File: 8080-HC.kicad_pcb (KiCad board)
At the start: 4 copper layers, 349 parts, among them U1 74HCU04, U10 74HC00, U11 74HC126, U12 74HC161, U13 74HC238, U14 74HC238, U15 74HC238, U16 74HC238, U17 74HC04, U178 74LS03, U18 74HC05, U181 74HC244, U182 74HC244, U19 74HC74, U194 74HC244, U195 74HC244, U2 74HC74, U20 74HC373, U21 74HC373, U215 74HC193, U216 74HC193, U217 74HC193, U218 74HC193, U22 74HC373, U23 74HC373, U239 74HC74, U24 74HC373, U242 74HC00, U243 74HCU04, U244 74HC00, U25 74HC244, U26 74HC244, U27 74HC244, U28 74HC244, U29 74HC244, U3 74HC00, U30 74HC373, U31 74HC373, U32 74HC244, U33 74HC244, U34 74HC244, U35 74HC244, U36 74HC373, U37 74HC373, U38 74HC244, U39 74HC244, U4 74HC04, U40 74HC244, U41 74HC244, U42 74HC245, U43 74HC04, U44 74HC04, U45 74LS373, U46 74HC04, U47 74HC04, U48 74HC04, U49 74HC04, U5 74HC00, U50 74HC04, U51 74HC04, U52 74HC04, U53 74HC238, U54 74HC238, U55 74HC238, U56 74HC238, U57 74HC04, U58 74HC04, U6 74HC04, U69 74HC05, U7 74HC05, U70 74LS05, U71 74HC04, U72 74LS126, U73 74LS126, U74 74LS126, U75 74LS126, U76 74LS126, U77 74HC00, U78 74HC00, U79 74HC04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

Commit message: finish routing the PC module
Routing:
- net iB6: track 52.8 -> 157.9 mm, vias 3 -> 8
- net iB5: track 86.3 -> 136.1 mm, vias 3 -> 5
- net Net-(L221-Pad2): track 12.5 -> 59.6 mm, vias 0 -> 5
- net Net-(L214-Pad2): track 12.5 -> 54.2 mm, vias 0 -> 2
- net Net-(L215-Pad2): track 12.9 -> 53.8 mm, vias 0 -> 3
- net Net-(L224-Pad2): track 21.7 -> 59.3 mm, vias 1 -> 2
- net iB1: track 97.0 -> 134.0 mm, vias 2 -> 3
- net Net-(L225-Pad2): track 28.5 -> 64.4 mm, vias 2 -> 5
- net Net-(L220-Pad2): track 51.0 -> 85.5 mm, vias 2 -> 4
- net Net-(L213-Pad2): track 29.0 -> 60.0 mm, vias 0 -> 2
- net Net-(L212-Pad2): track 42.0 -> 71.8 mm, vias 2 -> 4
- net Net-(L210-Pad2): track 56.4 -> 85.1 mm, vias 2 -> 3
- net Net-(L223-Pad2): track 31.9 -> 56.9 mm, vias 2 -> 4
- net Net-(L211-Pad2): track 47.7 -> 72.0 mm, vias 1 -> 2
- net Net-(L216-Pad2): track 33.8 -> 55.4 mm, vias 2 -> 3
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
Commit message: start routing the OPcode register, we have a piece of the iBn bus
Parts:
- removed D107, D109, D111, D114, D117, D120, D123, D125: LED_Small_ALT, LED_THT:LED_D3.0mm
- added L264: LED_Small_ALT, LED_THT:LED_D3.0mm, F.Cu at (-174.6, -19.1)
- added L265: LED_Small_ALT, LED_THT:LED_D3.0mm, F.Cu at (-170.1, -19.1)
- added L266: LED_Small_ALT, LED_THT:LED_D3.0mm, F.Cu at (-165.5, -19.1)
- added L267: LED_Small_ALT, LED_THT:LED_D3.0mm, F.Cu at (-160.9, -19.1)
- added L268: LED_Small_ALT, LED_THT:LED_D3.0mm, F.Cu at (-156.3, -19.1)
- added L269: LED_Small_ALT, LED_THT:LED_D3.0mm, F.Cu at (-151.8, -19.1)
- added L270: LED_Small_ALT, LED_THT:LED_D3.0mm, F.Cu at (-147.2, -19.1)
- added L271: LED_Small_ALT, LED_THT:LED_D3.0mm, F.Cu at (-142.6, -19.1)
- B37: renamed from RN17; value R_Network08 -> 22K
- moved B37 504.1 mm to (-148.6, -26.7), turned to 180 degrees
- moved U234 481.8 mm to (-170.2, -30.5), turned to 90 degrees
- moved D7 270.2 mm to (-130.0, -214.0)
- moved D79 270.2 mm to (66.2, -291.1)
- moved D85 270.2 mm to (65.9, -296.6)
- moved R19 270.2 mm to (46.6, -297.4)
- moved U36 270.2 mm to (76.1, -324.3)
- moved U58 270.2 mm to (146.5, -324.3)
- moved U90 270.2 mm to (70.9, -257.1)
- moved C1 270.2 mm to (-126.8, -281.7)
- moved C4 270.2 mm to (-10.9, -155.6)
- moved D1 270.2 mm to (-108.3, -237.8)
- moved D10 270.2 mm to (-83.5, -259.0)
- moved D100 270.2 mm to (-92.4, -298.7)
- moved D101 270.2 mm to (-98.3, -293.1)
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- renumbered U45 to U234
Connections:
- B38 pad 2: (no net) -> Net-(B38-Pad2)
- B38 pad 3: (no net) -> Net-(B38-Pad3)
- B38 pad 4: (no net) -> Net-(B38-Pad4)
- B38 pad 5: (no net) -> Net-(B38-Pad5)
- B38 pad 8: (no net) -> Net-(B38-Pad8)
- B38 pad 9: (no net) -> Net-(B38-Pad9)
- L218 pad 1: (no net) -> Net-(L218-Pad1)
- L277 pad 1: (no net) -> BUSAK
- RN15 pad 2: /I/O regs/iB0 -> iB0
- RN15 pad 3: /I/O regs/iB1 -> iB1
- RN15 pad 4: /I/O regs/iB2 -> iB2
- RN15 pad 5: /I/O regs/iB3 -> iB3
- RN15 pad 6: /I/O regs/iB4 -> iB4
- RN15 pad 7: /I/O regs/iB5 -> iB5
- RN15 pad 8: /I/O regs/iB6 -> iB6
- RN15 pad 9: /I/O regs/iB7 -> iB7
- U10 pad 10: (no net) -> Net-(U10-Pad10)
- U10 pad 11: (no net) -> Net-(U10-Pad11)
- U10 pad 12: (no net) -> Net-(U10-Pad12)
- U10 pad 13: (no net) -> Net-(U10-Pad13)
- U10 pad 8: (no net) -> Net-(U10-Pad8)
- U10 pad 9: (no net) -> Net-(U10-Pad9)
- U11 pad 1: (no net) -> Net-(U11-Pad1)
- U11 pad 11: (no net) -> /Timings Generator/QC
- U11 pad 3: (no net) -> /Timings Generator/QA
- U11 pad 6: (no net) -> /Timings Generator/QB
- U11 pad 8: (no net) -> /Timings Generator/QD
- U12 pad 2: (no net) -> /Timings Generator/CLK
- U13 pad 10: (no net) -> Net-(U13-Pad10)
- U13 pad 11: (no net) -> Net-(U13-Pad11)
- U13 pad 12: (no net) -> Net-(U13-Pad12)
- U13 pad 13: (no net) -> /Timings Generator/W2
- U13 pad 14: (no net) -> /Timings Generator/W1
- U13 pad 15: (no net) -> /Timings Generator/W0
- U13 pad 7: (no net) -> Net-(U13-Pad7)
- U13 pad 9: (no net) -> Net-(U13-Pad9)
- U14 pad 10: (no net) -> Net-(U14-Pad10)
- U14 pad 11: (no net) -> Net-(U14-Pad11)
- U14 pad 12: (no net) -> Net-(U14-Pad12)
- U14 pad 13: (no net) -> /Timings Generator/M2
- U14 pad 14: (no net) -> Net-(U14-Pad14)
- U14 pad 15: (no net) -> Net-(U14-Pad15)
- U14 pad 7: (no net) -> Net-(U14-Pad7)
- U14 pad 9: (no net) -> Net-(U14-Pad9)
- U15 pad 10: (no net) -> Net-(U15-Pad10)
- U15 pad 11: (no net) -> /Timings Generator/T12
- U15 pad 12: (no net) -> Net-(U15-Pad12)
- U15 pad 13: (no net) -> /Timings Generator/T10
- U15 pad 14: (no net) -> /Timings Generator/T9
- U15 pad 15: (no net) -> /Timings Generator/T8
- U15 pad 7: (no net) -> Net-(U15-Pad7)
- U15 pad 9: (no net) -> Net-(U15-Pad9)
- U16 pad 10: (no net) -> /Timings Generator/T5
- U16 pad 11: (no net) -> /Timings Generator/T4
- U16 pad 12: (no net) -> /Timings Generator/T3
- U16 pad 13: (no net) -> /Timings Generator/T2
- U16 pad 14: (no net) -> /Timings Generator/T1
- U16 pad 15: (no net) -> /Timings Generator/T0
- U16 pad 7: (no net) -> /Timings Generator/T7
- U16 pad 9: (no net) -> /Timings Generator/T6
- U17 pad 12: (no net) -> Net-(U17-Pad12)
- U17 pad 13: (no net) -> Net-(U17-Pad13)
- U178 pad 4: (no net) -> PCCKdE
- U178 pad 5: (no net) -> T3
- U18 pad 10: (no net) -> Net-(U18-Pad10)
- U18 pad 11: (no net) -> Net-(U18-Pad11)
- U18 pad 12: (no net) -> Net-(U18-Pad12)
- U18 pad 13: (no net) -> Net-(U18-Pad13)
- U18 pad 4: (no net) -> /regs_decode/dataOUT
- U18 pad 8: (no net) -> /regs_decode/memRD
- U181 pad 12: (no net) -> /Program Counter/A11
- U181 pad 14: (no net) -> /Program Counter/A10
- U181 pad 16: (no net) -> /Program Counter/A9
- U181 pad 18: (no net) -> /Program Counter/A8
- U181 pad 3: (no net) -> /Program Counter/A12
- U181 pad 5: (no net) -> /Program Counter/A13
- U181 pad 7: (no net) -> /Program Counter/A14
- U181 pad 9: (no net) -> Net-(U181-Pad9)
- U182 pad 12: (no net) -> /Program Counter/A3
- U182 pad 14: (no net) -> /Program Counter/A2
- U182 pad 16: (no net) -> /Program Counter/A1
- U182 pad 18: (no net) -> /Program Counter/A0
- U182 pad 3: (no net) -> /Program Counter/A4
- U182 pad 5: (no net) -> /Program Counter/A5
- U182 pad 7: (no net) -> /Program Counter/A6
- U182 pad 9: (no net) -> /Program Counter/A7
- U19 pad 10: (no net) -> Net-(U19-Pad10)
- U19 pad 11: (no net) -> Net-(U19-Pad11)
- U19 pad 12: (no net) -> Net-(U19-Pad12)
- U19 pad 13: (no net) -> Net-(U19-Pad13)
- U19 pad 5: (no net) -> Net-(U19-Pad5)
- U19 pad 8: (no net) -> Net-(U19-Pad8)
- U19 pad 9: (no net) -> Net-(U19-Pad9)
- U2 pad 9: (no net) -> Net-(U2-Pad9)
- U20 pad 11: (no net) -> /regs_A_B_C_D_E/AregWR
- U21 pad 11: (no net) -> /regs_A_B_C_D_E/BregWR
- U215 pad 12: (no net) -> Net-(U215-Pad12)
- U215 pad 13: (no net) -> Net-(U215-Pad13)
- U216 pad 12: (no net) -> Net-(U216-Pad12)
- U217 pad 12: (no net) -> Net-(U217-Pad12)
- U218 pad 12: (no net) -> Net-(U218-Pad12)
- U22 pad 11: (no net) -> /regs_A_B_C_D_E/CregWR
- U23 pad 11: (no net) -> /regs_A_B_C_D_E/DregWR
- U234 pad 11: (no net) -> /I/O regs/T1
- U234 pad 12: /I/O regs/OP4 -> OP4
- U234 pad 13: /I/O regs/iB4 -> iB4
- U234 pad 14: /I/O regs/iB5 -> iB5
- U234 pad 15: /I/O regs/OP5 -> OP5
- U234 pad 16: /I/O regs/OP6 -> OP6
- U234 pad 17: /I/O regs/iB6 -> iB6
- U234 pad 18: /I/O regs/iB7 -> iB7
- U234 pad 19: /I/O regs/OP7 -> OP7
- U234 pad 2: /I/O regs/OP0 -> OP0
- U234 pad 3: /I/O regs/iB0 -> iB0
- U234 pad 4: /I/O regs/iB1 -> iB1
- U234 pad 5: /I/O regs/OP1 -> OP1
- U234 pad 6: /I/O regs/OP2 -> OP2
- U234 pad 7: /I/O regs/iB2 -> iB2
- U234 pad 8: /I/O regs/iB3 -> iB3
- U234 pad 9: /I/O regs/OP3 -> OP3
- U24 pad 11: (no net) -> /regs_A_B_C_D_E/EregWR
- U242 pad 8: (no net) -> CLK
- U244 pad 11: (no net) -> CLK2
- U244 pad 3: (no net) -> /I/O control/DataDIR
- U3 pad 10: (no net) -> /HALT/T2
- U3 pad 9: (no net) -> /HALT/HALT
- U30 pad 11: (no net) -> /regs_HL/HregWR
- U31 pad 11: (no net) -> /regs_HL/LregWR
- U32 pad 12: (no net) -> /regs_HL/A12
- U32 pad 14: (no net) -> /regs_HL/A13
- U32 pad 16: (no net) -> /regs_HL/A14
- U32 pad 18: (no net) -> /regs_HL/A15
- U32 pad 3: (no net) -> /regs_HL/A11
- U32 pad 5: (no net) -> /regs_HL/A10
- U32 pad 7: (no net) -> /regs_HL/A9
- U32 pad 9: (no net) -> /regs_HL/A8
- U34 pad 12: (no net) -> /regs_HL/A4
- U34 pad 14: (no net) -> /regs_HL/A5
- U34 pad 16: (no net) -> /regs_HL/A6
- U34 pad 18: (no net) -> /regs_HL/A7
- U34 pad 3: (no net) -> /regs_HL/A3
- U34 pad 5: (no net) -> /regs_HL/A2
- U34 pad 7: (no net) -> /regs_HL/A1
- U34 pad 9: (no net) -> /regs_HL/A0
- U36 pad 11: (no net) -> /reg_WK/WKHregWR
- U37 pad 11: (no net) -> /reg_WK/WKLregWR
- U38 pad 12: (no net) -> /reg_WK/A12
- U38 pad 14: (no net) -> /reg_WK/A13
- U38 pad 16: (no net) -> /reg_WK/A14
- U38 pad 18: (no net) -> /reg_WK/A15
- U38 pad 3: (no net) -> /reg_WK/A11
- U38 pad 5: (no net) -> /reg_WK/A10
- U38 pad 7: (no net) -> /reg_WK/A9
- U38 pad 9: (no net) -> /reg_WK/A8
- U4 pad 10: (no net) -> Net-(U4-Pad10)
- U4 pad 11: (no net) -> Net-(U4-Pad11)
- U4 pad 12: (no net) -> Net-(U4-Pad12)
- U4 pad 13: (no net) -> Net-(U4-Pad13)
- U4 pad 5: (no net) -> Net-(U4-Pad5)
- U4 pad 6: (no net) -> Net-(U4-Pad6)
- U4 pad 8: (no net) -> Net-(U4-Pad8)
- U4 pad 9: (no net) -> Net-(U4-Pad9)
- U40 pad 12: (no net) -> /reg_WK/A4
- U40 pad 14: (no net) -> /reg_WK/A5
- U40 pad 16: (no net) -> /reg_WK/A6
- U40 pad 18: (no net) -> /reg_WK/A7
- U40 pad 3: (no net) -> /reg_WK/A3
- U40 pad 5: (no net) -> /reg_WK/A2
- U40 pad 7: (no net) -> /reg_WK/A1
- U40 pad 9: (no net) -> /reg_WK/A0
- U42 pad 1: (no net) -> /I/O regs/DataDIR
- U42 pad 11: /I/O regs/iB7 -> iB7
- U42 pad 12: /I/O regs/iB6 -> iB6
- U42 pad 13: /I/O regs/iB5 -> iB5
- U42 pad 14: /I/O regs/iB4 -> iB4
- U42 pad 15: /I/O regs/iB3 -> iB3
- U42 pad 16: /I/O regs/iB2 -> iB2
- U42 pad 17: /I/O regs/iB1 -> iB1
- U42 pad 18: /I/O regs/iB0 -> iB0
- U42 pad 19: (no net) -> /I/O regs/DataG
- U46 pad 11: /I/O regs/iB4 -> iB4
- U46 pad 13: /I/O regs/iB5 -> iB5
- U46 pad 5: /I/O regs/iB2 -> iB2
- U46 pad 9: /I/O regs/iB3 -> iB3
- U48 pad 1: /I/O regs/iB0 -> iB0
- U48 pad 10: (no net) -> /regs_decode/PCLregWR
- U48 pad 12: (no net) -> /regs_decode/SPHregWR
- U48 pad 3: /I/O regs/iB1 -> iB1
- U48 pad 8: (no net) -> /regs_decode/PCHregWR
- U49 pad 1: /I/O regs/iB6 -> iB6
- U49 pad 3: /I/O regs/iB7 -> iB7
- U52 pad 1: (no net) -> /regs_decode/T0
- U53 pad 10: (no net) -> /regs_decode/LregWR
- U53 pad 11: (no net) -> /regs_decode/HregWR
- U53 pad 12: (no net) -> /regs_decode/EregWR
- U53 pad 13: (no net) -> /regs_decode/DregWR
- U53 pad 14: (no net) -> /regs_decode/CregWR
- U53 pad 15: (no net) -> /regs_decode/BregWR
- U53 pad 7: (no net) -> /regs_decode/AregWR
- U54 pad 14: (no net) -> /regs_decode/FregWR
- U54 pad 15: (no net) -> Net-(U54-Pad15)
- U54 pad 7: (no net) -> /regs_decode/WKLregWR
- U54 pad 9: (no net) -> /regs_decode/WKHregWR
- U55 pad 10: (no net) -> /regs_decode/LregRD
- U55 pad 11: (no net) -> /regs_decode/HregRD
- U55 pad 12: (no net) -> /regs_decode/EregRD
- U55 pad 13: (no net) -> /regs_decode/DregRD
- U55 pad 14: (no net) -> /regs_decode/CregRD
- U55 pad 15: (no net) -> /regs_decode/BregRD
- U55 pad 7: (no net) -> /regs_decode/AregRD
- U56 pad 10: (no net) -> /regs_decode/SPLregRD
- U56 pad 11: (no net) -> /regs_decode/SPHregRD
- U56 pad 12: (no net) -> /regs_decode/PCLregRD
- U56 pad 13: (no net) -> /regs_decode/PCHregRD
- U56 pad 14: (no net) -> /regs_decode/FregRD
- U56 pad 15: (no net) -> Net-(U56-Pad15)
- U56 pad 7: (no net) -> /regs_decode/WKLregRD
- U56 pad 9: (no net) -> /regs_decode/WKHregRD
- U57 pad 2: (no net) -> /regs_decode/SPLregWR
- U58 pad 3: (no net) -> /regs_decode/Qa
- U6 pad 14: (no net) -> Net-(U6-Pad14)
- U6 pad 4: (no net) -> /Reset/reset(inner)
- U6 pad 7: (no net) -> Net-(U6-Pad7)
- U69 pad 1: (no net) -> /I/O control/W0
- U69 pad 8: (no net) -> /MOV / MVI/s3
- U7 pad 10: (no net) -> /Reset/INTclr
- U7 pad 2: (no net) -> /Reset/OUTdE
- U7 pad 6: (no net) -> /Reset/HLTclr
- U7 pad 8: (no net) -> /Reset/IEFclr
- U77 pad 3: (no net) -> /I/O control/DataG
- U78 pad 3: (no net) -> /I/O control/PCADout
- U79 pad 1: (no net) -> /MOV / MVI/OP7
- U8 pad 1: (no net) -> /BUSRQ/T3
- U80 pad 11: (no net) -> /MOV / MVI/PCsel
- U82 pad 8: (no net) -> /MOV / MVI/HALT
- U83 pad 10: (no net) -> /MOV / MVI/T8
- U83 pad 11: (no net) -> /MOV / MVI/d3
- U83 pad 5: (no net) -> /MOV / MVI/T5
- U83 pad 6: (no net) -> /MOV / MVI/PCinc
- U84 pad 11: (no net) -> /HALT/MCLR
- U84 pad 13: (no net) -> /HALT/T4
- U84 pad 5: (no net) -> /MOV / MVI/M3
- U85 pad 4: (no net) -> /MOV / MVI/HLTA
- U87 pad 11: (no net) -> /MOV / MVI/s2
- U87 pad 3: (no net) -> /MOV / MVI/d2
- U87 pad 6: (no net) -> /MOV / MVI/d1
- U87 pad 8: (no net) -> /MOV / MVI/d0
- U88 pad 3: (no net) -> /MOV / MVI/s1
- U88 pad 6: (no net) -> /MOV / MVI/s0
- U89 pad 8: (no net) -> /INR / DCR decode/LXI
- U9 pad 2: (no net) -> /BUSRQ/Mstop
- U9 pad 4: (no net) -> /BUSRQ/OUTdE
- U91 pad 2: (no net) -> /HALT/HLTclr
- U92 pad 1: (no net) -> /INR / DCR decode/OP0
- U92 pad 10: (no net) -> /INR / DCR decode/DCR
- U92 pad 11: (no net) -> /INR / DCR decode/INR
- U92 pad 12: (no net) -> /INR / DCR decode/INX-DCX
- U92 pad 13: (no net) -> Net-(U92-Pad13)
- U92 pad 15: (no net) -> Net-(U92-Pad15)
- U92 pad 2: (no net) -> /INR / DCR decode/OP1
- U92 pad 3: (no net) -> /INR / DCR decode/OP2
- U92 pad 4: (no net) -> /INR / DCR decode/OP6
- U92 pad 5: (no net) -> /INR / DCR decode/OP7
- U92 pad 7: (no net) -> Net-(U92-Pad7)
- U92 pad 9: (no net) -> Net-(U92-Pad9)
- U93 pad 1: (no net) -> /INR / DCR decode/OP3
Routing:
- net iB6: track 157.9 -> 269.2 mm, vias 8 -> 10
- net iB4: track 107.3 -> 210.3 mm, vias 4 -> 7
- net iB2: track 130.8 -> 232.7 mm, vias 3 -> 5
- net iB3: track 119.2 -> 219.8 mm, vias 4 -> 6
- net iB5: track 136.1 -> 230.1 mm, vias 5 -> 7
- net iB7: track 123.2 -> 212.3 mm, vias 5 -> 6
- net iB0: track 133.5 -> 210.6 mm, vias 6 -> 7
- net iB1: track 134.0 -> 205.3 mm, vias 3 -> 5
- net OP0: track 0.00 -> 33.7 mm, vias 0 -> 1
- net Net-(L226-Pad2): track 39.4 -> 68.7 mm, vias 2 -> 7
- net OP1: track 0.00 -> 28.7 mm, vias 0 -> 2
- net OP2: track 0.00 -> 13.5 mm, vias 0 -> 1
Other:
- board text added: "OPcode register"

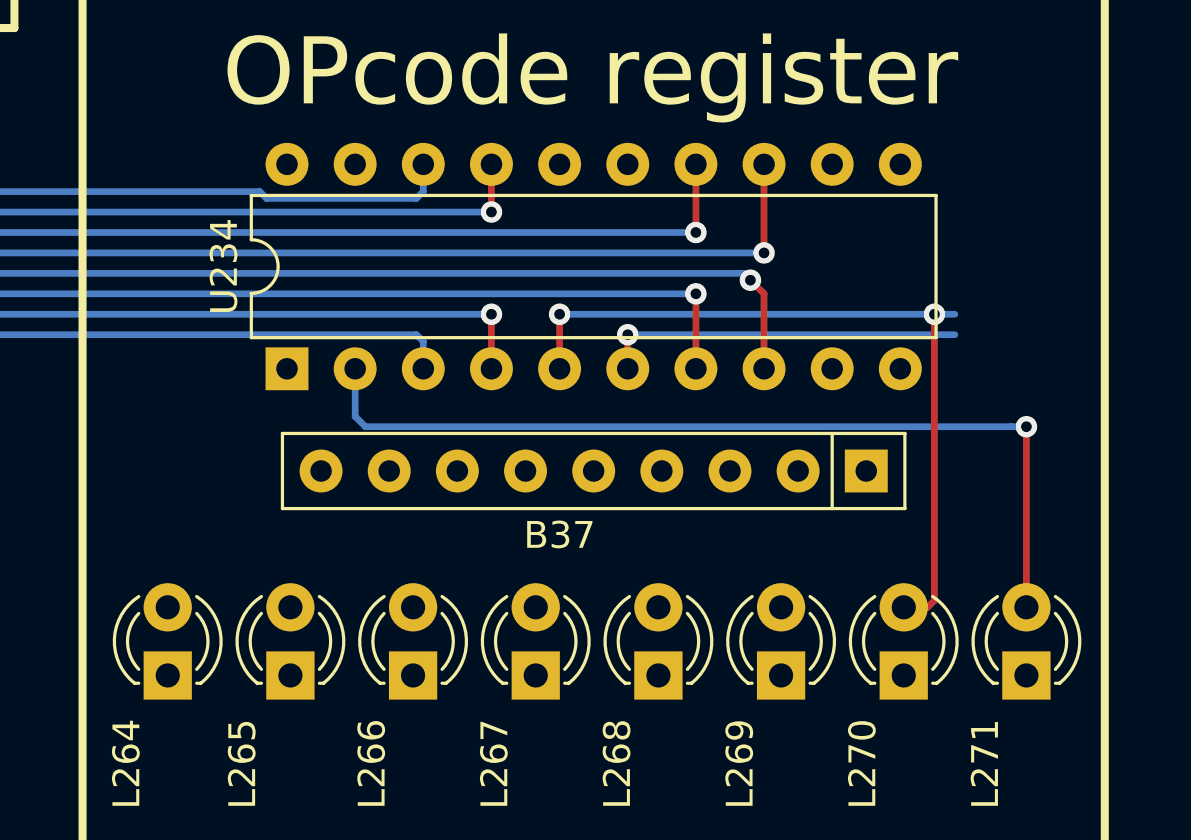
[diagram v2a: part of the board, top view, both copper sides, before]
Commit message: OPcode register block completely routed
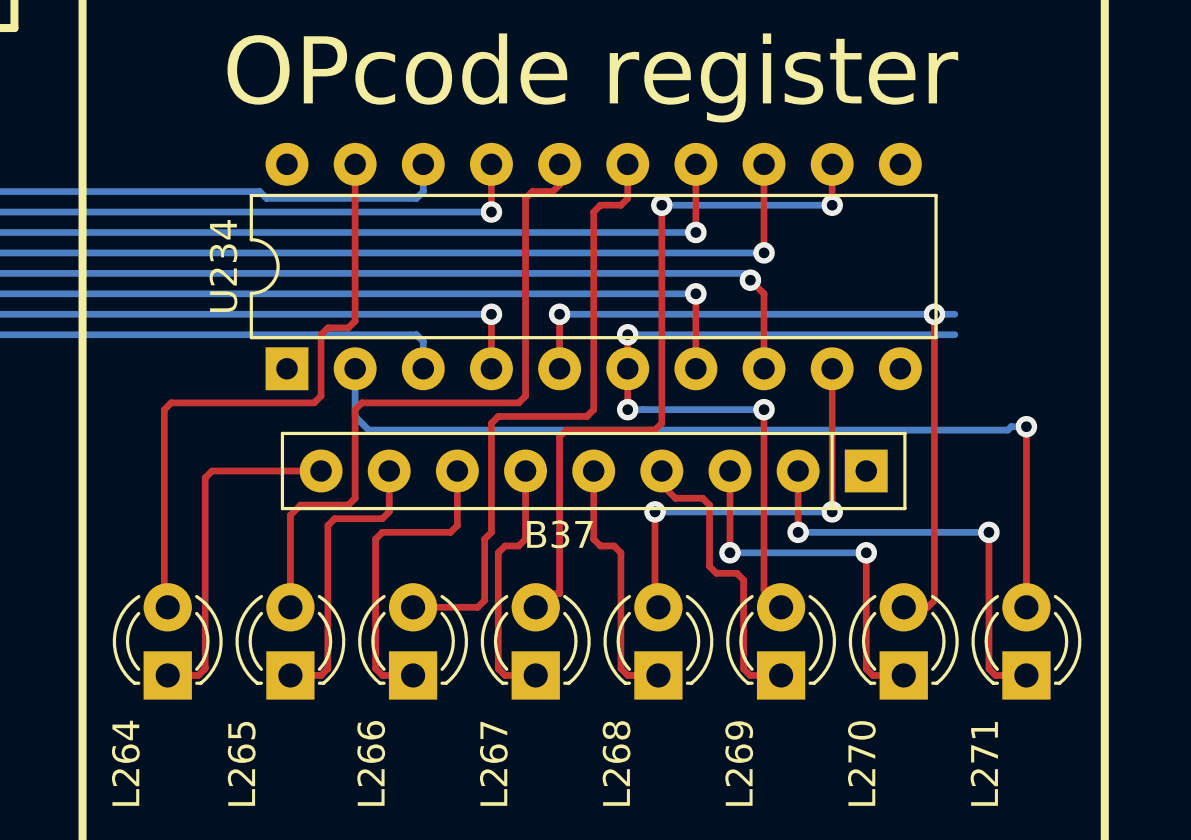
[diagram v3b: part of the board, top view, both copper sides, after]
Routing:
- net OP4: track 0.00 -> 27.0 mm, vias 0 -> 2
- net OP6: track 0.00 -> 25.6 mm
- net OP5: track 0.00 -> 23.6 mm
- net OP7: track 0.00 -> 23.1 mm
- net Net-(B37-Pad2): track 0.00 -> 16.0 mm, vias 0 -> 2
- net OP3: track 0.00 -> 15.5 mm, vias 0 -> 2
- net OP2: track 13.5 -> 27.7 mm, vias 1 -> 3
- net Net-(B37-Pad3): track 0.00 -> 14.0 mm, vias 0 -> 2
- net Net-(B37-Pad9): track 0.00 -> 13.0 mm
- net Net-(B37-Pad7): track 0.00 -> 11.6 mm
- net Net-(B37-Pad4): track 0.00 -> 11.2 mm
- net Net-(B37-Pad8): track 0.00 -> 10.9 mm
- net Net-(B37-Pad6): track 0.00 -> 9.59 mm
- net Net-(B37-Pad5): track 0.00 -> 9.59 mm

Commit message: place leds and inverters for the iBn bus
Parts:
- added U46: 74HC04, Package_DIP:DIP-14_W7.62mm, F.Cu at (-228.6, -261.6)
- added U48: 74HC04, Package_DIP:DIP-14_W7.62mm, F.Cu at (-228.6, -237.4)
- added U49: 74HC04, Package_DIP:DIP-14_W7.62mm, F.Cu at (-217.8, -237.4)
- B31, B32, B37: value 22K -> 2.2K
- B35: renamed from RN13; value R_Network08 -> 2.2K
- B36: renamed from RN18; value R_Network08 -> 2.2K
- B41: renamed from RN11; value R_Network08 -> 1K
- B5: renamed from RN15; value R_Network08 -> 1K
- moved L259 325.2 mm to (-211.3, -6.35), turned to 90 degrees
- moved L256 323.7 mm to (-225.0, -6.35), turned to 90 degrees
- moved U232 323.3 mm to (-215.9, -17.8), turned to 90 degrees
- moved L262 315.9 mm to (-197.6, -6.35), turned to 90 degrees
- moved L258 313.0 mm to (-215.9, -6.35), turned to 90 degrees
- moved L257 312.5 mm to (-220.5, -6.35), turned to 90 degrees
- moved B36 312.1 mm to (-195.6, -14.0), turned to 180 degrees
- moved L261 304.7 mm to (-202.2, -6.35), turned to 90 degrees
- moved B41 301.7 mm to (-436.9, -284.5), turned to 90 degrees
- moved U231 301.6 mm to (-241.3, -30.5), turned to 90 degrees
- moved L263 297.3 mm to (-193.0, -6.35), turned to 90 degrees
- moved L260 284.1 mm to (-206.8, -6.35), turned to 90 degrees
- moved U233 269.5 mm to (-195.6, -17.8), turned to 90 degrees
- moved B5 194.6 mm to (-361.9, -316.2)
- renumbered D128 to L256, D127 to L257, D126 to L258, D124 to L259, D121 to L260, D118 to L261, D115 to L262, D112 to L263, U42 to U231, U46 to U232, U48 to U233
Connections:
- net /I/O regs/DataDIR renamed DataDIR
- net /I/O regs/DataG renamed DataG
- net /I/O regs/io_D0 renamed io_D0
- net /I/O regs/io_D1 renamed io_D1
- net /I/O regs/io_D2 renamed io_D2
- net /I/O regs/io_D3 renamed io_D3
- net /I/O regs/io_D4 renamed io_D4
- net /I/O regs/io_D5 renamed io_D5
- net /I/O regs/io_D6 renamed io_D6
- net /I/O regs/io_D7 renamed io_D7
- L256 pad 1: Net-(D128-Pad1) -> Net-(L256-Pad1)
- L257 pad 1: Net-(D127-Pad1) -> Net-(L257-Pad1)
- L258 pad 1: Net-(D126-Pad1) -> Net-(L258-Pad1)
- L260 pad 1: Net-(D121-Pad1) -> Net-(L260-Pad1)
- L261 pad 1: Net-(D118-Pad1) -> Net-(L261-Pad1)
- L262 pad 1: Net-(D115-Pad1) -> Net-(L262-Pad1)
- L263 pad 1: Net-(D112-Pad1) -> Net-(L263-Pad1)
- U232 pad 1: /I/O regs/A8 -> iB7
- U232 pad 12: Net-(D126-Pad1) -> Net-(L257-Pad1)
- U232 pad 13: iB5 -> iB6
- U232 pad 2: Net-(D105-Pad1) -> Net-(L256-Pad1)
- U232 pad 3: /I/O regs/A9 -> iB5
- U232 pad 4: Net-(D106-Pad1) -> Net-(L258-Pad1)
- U232 pad 5: iB2 -> iB3
- U232 pad 6: Net-(D118-Pad1) -> Net-(L260-Pad1)
- U232 pad 8: Net-(D121-Pad1) -> Net-(L261-Pad1)
- U232 pad 9: iB3 -> iB2
- U233 pad 1: iB0 -> iB1
- U233 pad 10: /regs_decode/PCLregWR -> (no net)
- U233 pad 11: Net-(U48-Pad11) -> (no net)
- U233 pad 12: /regs_decode/SPHregWR -> Net-(L263-Pad1)
- U233 pad 13: Net-(U48-Pad13) -> iB0
- U233 pad 2: Net-(D112-Pad1) -> Net-(L262-Pad1)
- U233 pad 3: iB1 -> (no net)
- U233 pad 4: Net-(D115-Pad1) -> (no net)
- U233 pad 5: Net-(U48-Pad5) -> (no net)
- U233 pad 6: /regs_decode/memWR -> (no net)
- U233 pad 8: /regs_decode/PCHregWR -> (no net)
- U233 pad 9: Net-(U48-Pad9) -> (no net)
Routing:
- net iB0: track 210.6 -> 241.7 mm, vias 7 -> 8
- net iB1: track 205.3 -> 236.2 mm, vias 5 -> 6
- net iB3: track 219.8 -> 233.8 mm
- net OP2: track 27.7 -> 14.2 mm, vias 3 -> 2
- net iB2: track 232.7 -> 245.0 mm
- net iB5: track 230.1 -> 238.0 mm
- net iB4: track 210.3 -> 218.0 mm
- net iB7: track 212.3 -> 218.5 mm
- net iB6: track 269.2 -> 271.4 mm, vias 10 -> 11
- net OP1: track 28.7 -> 27.9 mm
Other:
- board text added: "OP0"
- board text added: "OP1"
- board text added: "OP2"
- board text added: "OP3"
- board text added: "OP4"
- board text added: "OP5"
- board text added: "OP6"
- board text added: "OP7"

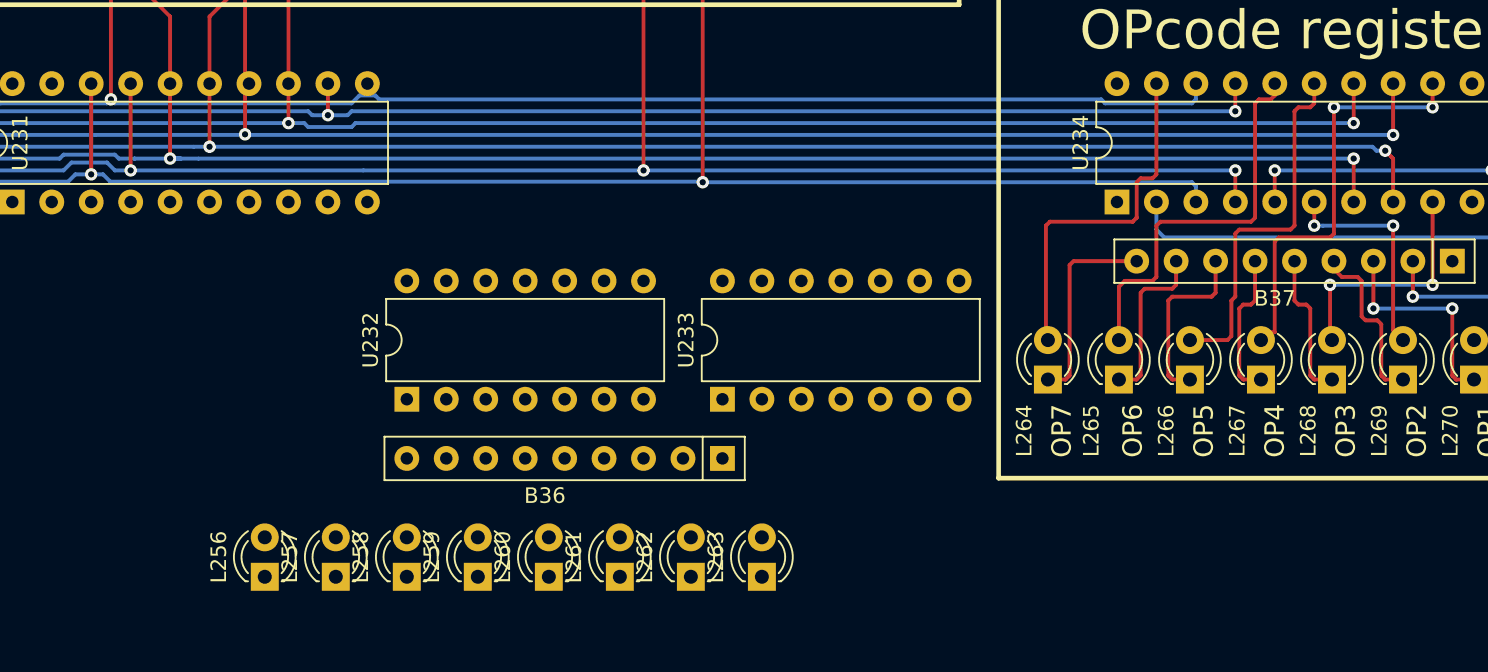
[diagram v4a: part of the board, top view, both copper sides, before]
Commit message: iBn bus inverters and leds completely routed
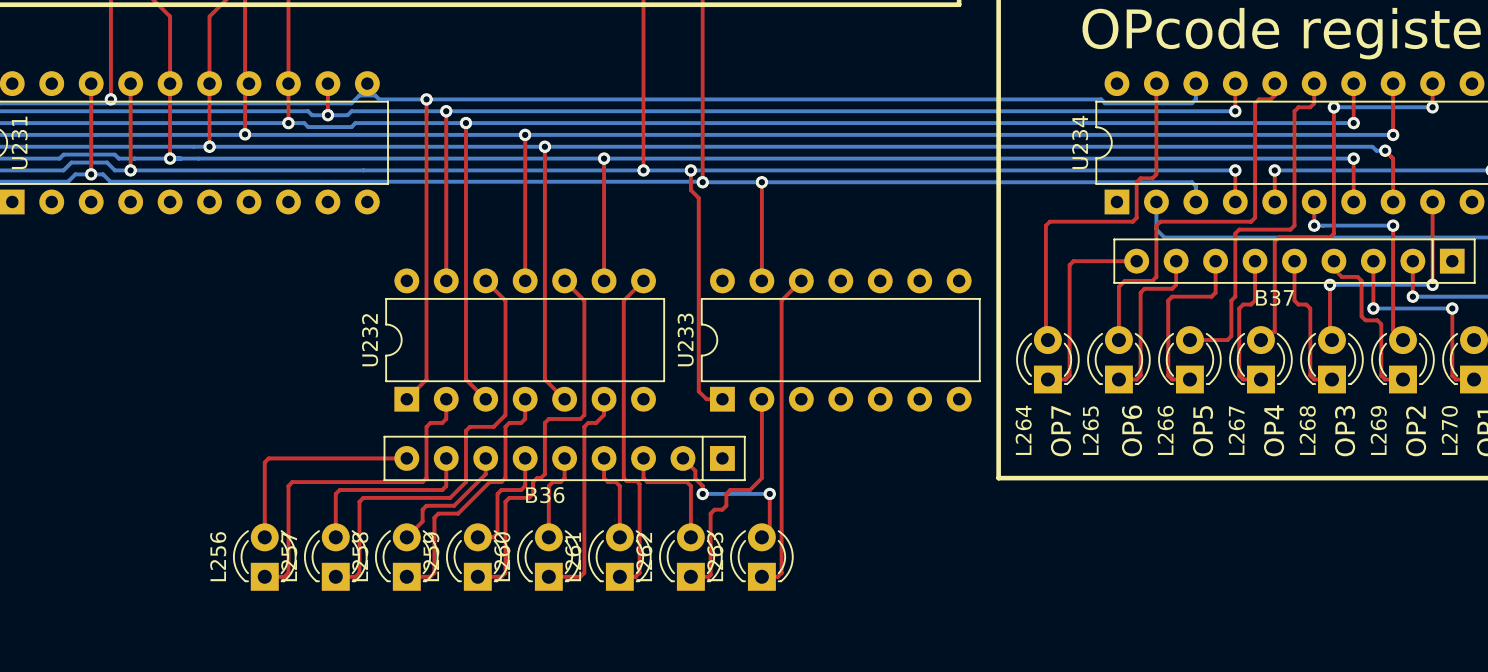
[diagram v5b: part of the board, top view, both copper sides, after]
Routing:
- net Net-(L257-Pad1): track 0.00 -> 29.0 mm
- net Net-(L259-Pad1): track 0.00 -> 25.4 mm
- net Net-(L256-Pad1): track 0.00 -> 22.4 mm
- net Net-(L261-Pad1): track 0.00 -> 21.5 mm
- net Net-(L263-Pad1): track 0.00 -> 20.7 mm
- net iB7: track 218.5 -> 238.4 mm, vias 6 -> 7
- net iB5: track 238.0 -> 256.3 mm, vias 7 -> 8
- net Net-(L258-Pad1): track 0.00 -> 17.3 mm
- net iB3: track 233.8 -> 250.6 mm, vias 6 -> 7
- net iB1: track 236.2 -> 252.4 mm, vias 6 -> 7
- net Net-(L262-Pad1): track 0.00 -> 15.0 mm
- net Net-(L260-Pad1): track 0.00 -> 14.4 mm
- net Net-(B36-Pad9): track 0.00 -> 14.1 mm
- net Net-(B36-Pad8): track 0.00 -> 11.9 mm
- net iB6: track 271.4 -> 282.3 mm, vias 11 -> 12
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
